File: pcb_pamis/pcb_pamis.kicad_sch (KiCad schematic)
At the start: 55 parts, among them J1 USB_C_Receptacle_USB2.0_16P, J10 Conn_01x03, J11 Conn_01x03, J12 Conn_02x06_Odd_Even, J13 1755736, J2 1755736, J6 Conn_01x05, J7 Conn_01x05, J8 Conn_01x05, J9 Conn_01x03, Q1 Q_NPN_BEC, Q2 Q_NPN_BEC, Q3 NMOS, Q4 NMOS, Q5 NMOS, SW1 SW_Push, U1 ESP32-WROOM-32UE, U2 CP2102N-Axx-xQFN28

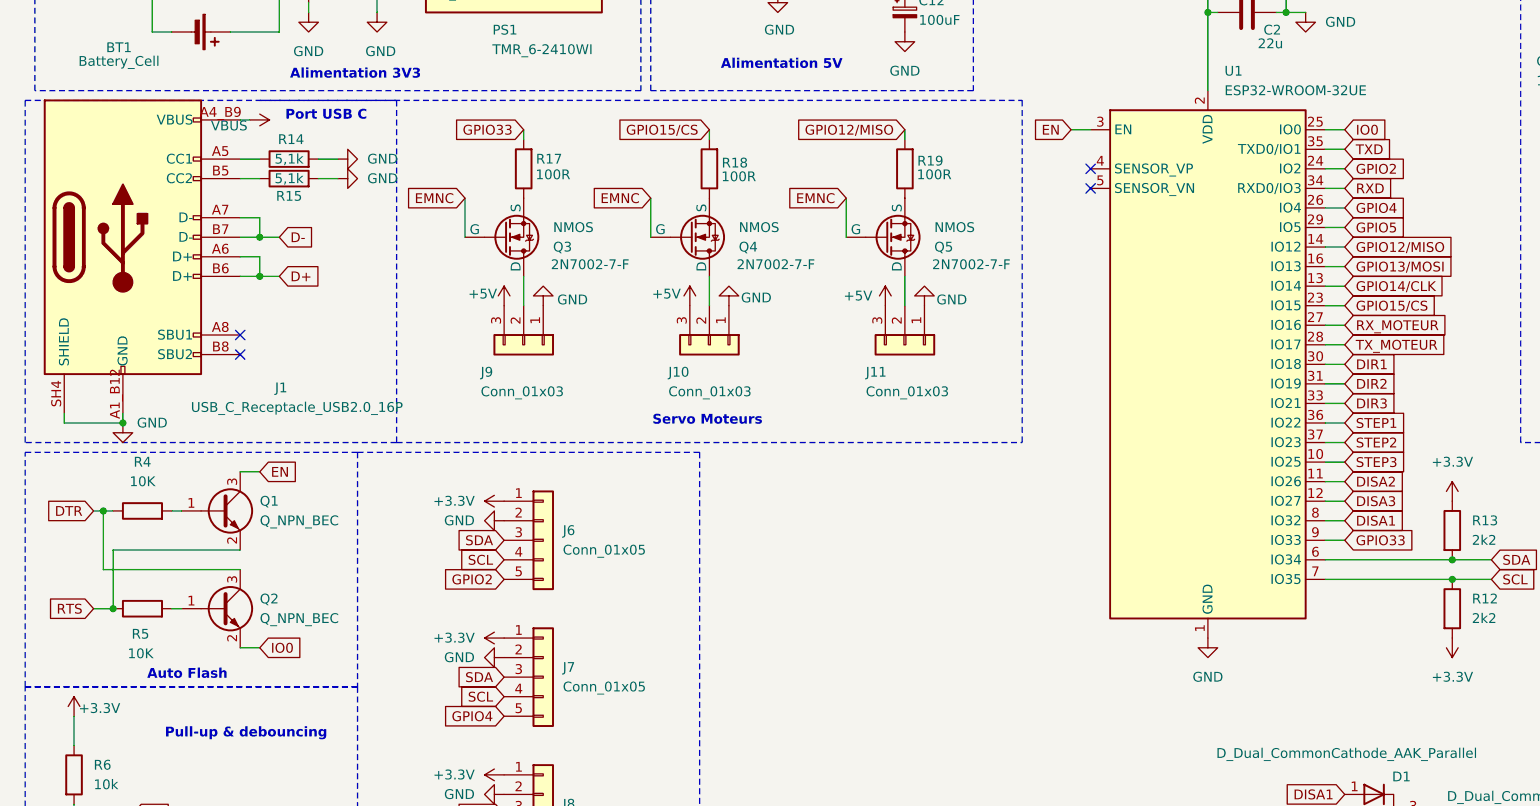
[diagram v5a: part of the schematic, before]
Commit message: correctif auto flash pcb pami
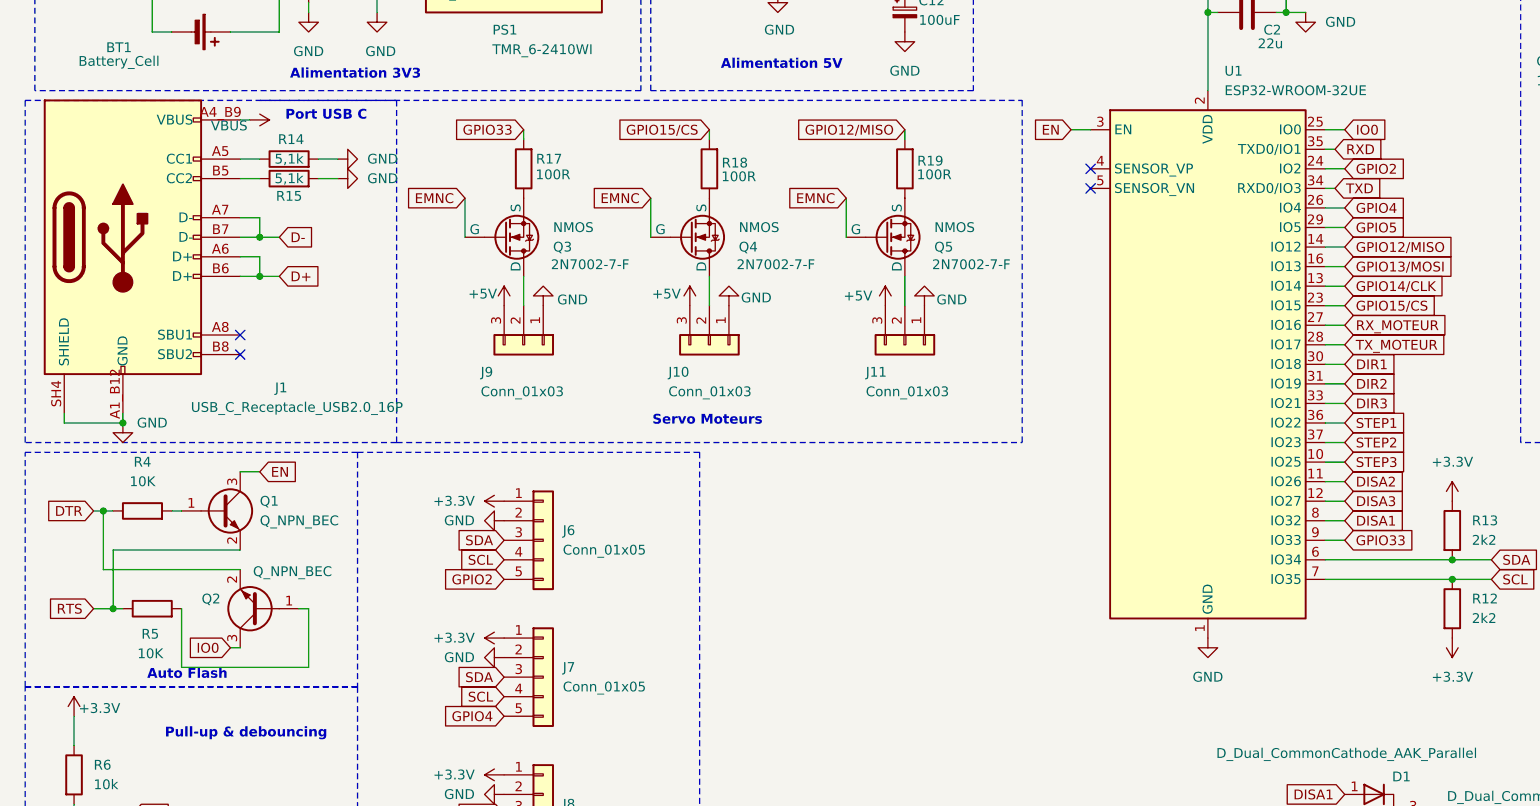
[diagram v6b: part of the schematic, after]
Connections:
- net DTR: now also Q2.2 (E); no longer Q2.3 (C)
- net IO0: now also Q2.3 (C); no longer Q2.2 (E)
- net RXD: now also U1.35 (TXD0/IO1); no longer U1.34 (RXD0/IO3)
- net TXD: now also U1.34 (RXD0/IO3); no longer U1.35 (TXD0/IO1)
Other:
- moved on the sheet: Q2, R5
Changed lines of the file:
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@@
 	(wire
 		(pts
-			(xy 182.88 60.96) (xy 185.42 60.96)
-		)
-		(stroke
-			(width 0)
-			(type default)
-		)
-	)
-	(wire
-		(pts
 			(xy 257.81 22.86) (xy 257.81 19.05)
 		)
@@
 	(wire
 		(pts
+			(xy 182.88 66.04) (xy 184.15 66.04)
+		)
+		(stroke
+			(width 0)
+			(type default)
+		)
+	)
+	(wire
+		(pts
 			(xy 22.86 191.77) (xy 22.86 193.04)
 		)
@@
 	(wire
 		(pts
-			(xy 41.91 125.73) (xy 44.45 125.73)
+			(xy 182.88 83.82) (xy 185.42 83.82)
 		)
 		(stroke
@@
 	(wire
 		(pts
-			(xy 182.88 83.82) (xy 185.42 83.82)
+			(xy 40.64 125.73) (xy 41.91 125.73)
 		)
 		(stroke
@@
 	(wire
 		(pts
+			(xy 50.8 120.65) (xy 50.8 128.27)
+		)
+		(stroke
+			(width 0)
+			(type default)
+		)
+	)
+	(wire
+		(pts
 			(xy 200.66 160.02) (xy 200.66 154.94)
 		)
@@
 	(wire
 		(pts
-			(xy 41.91 115.57) (xy 24.13 115.57)
-		)
-		(stroke
-			(width 0)
-			(type default)
-		)
-	)
-	(wire
-		(pts
 			(xy 128.27 40.64) (xy 128.27 36.83)
 		)
@@
 	(wire
 		(pts
+			(xy 50.8 128.27) (xy 34.29 128.27)
+		)
+		(stroke
+			(width 0)
+			(type default)
+		)
+	)
+	(wire
+		(pts
 			(xy 182.88 149.86) (xy 158.75 149.86)
 		)
@@
 	(wire
 		(pts
-			(xy 182.88 66.04) (xy 185.42 66.04)
+			(xy 182.88 60.96) (xy 184.15 60.96)
 		)
 		(stroke
@@
 	(wire
 		(pts
+			(xy 24.13 115.57) (xy 41.91 115.57)
+		)
+		(stroke
+			(width 0)
+			(type default)
+		)
+	)
+	(wire
+		(pts
 			(xy 185.42 68.58) (xy 182.88 68.58)
 		)
@@
 	(wire
 		(pts
+			(xy 34.29 128.27) (xy 34.29 120.65)
+		)
+		(stroke
+			(width 0)
+			(type default)
+		)
+	)
+	(wire
+		(pts
+			(xy 26.67 120.65) (xy 25.4 120.65)
+		)
+		(stroke
+			(width 0)
+			(type default)
+		)
+	)
+	(wire
+		(pts
 			(xy 78.74 58.42) (xy 78.74 59.69)
 		)
@@
 	(wire
 		(pts
-			(xy 33.02 120.65) (xy 34.29 120.65)
-		)
-		(stroke
-			(width 0)
-			(type default)
-		)
-	)
-	(wire
-		(pts
 			(xy 265.43 22.86) (xy 265.43 26.67)
 		)
@@
 	(wire
 		(pts
+			(xy 49.53 120.65) (xy 50.8 120.65)
+		)
+		(stroke
+			(width 0)
+			(type default)
+		)
+	)
+	(wire
+		(pts
 			(xy 232.41 157.48) (xy 231.14 157.48)
 		)
@@
 	(global_label "IO0"
 		(shape input)
-		(at 44.45 125.73 0)
+		(at 40.64 125.73 180)
 		(fields_autoplaced yes)
 		(effects
@@
 				(size 1.27 1.27)
 			)
-			(justify left)
+			(justify right)
 		)
 		(property "Intersheetrefs" "${INTERSHEET_REFS}"
-			(at 50.58 125.73 0)
+			(at 34.51 125.73 0)
 			(effects
 				(font
 					(size 1.27 1.27)
 				)
-				(justify left)
+				(justify right)
 				(hide yes)
 			)
@@
 	(global_label "TXD"
 		(shape input)
-		(at 185.42 60.96 0)
+		(at 184.15 66.04 0)
 		(fields_autoplaced yes)
 		(effects
@@
 		)
 		(property "Intersheetrefs" "${INTERSHEET_REFS}"
-			(at 191.8523 60.96 0)
+			(at 190.5823 66.04 0)
 			(effects
 				(font
@@
 	(global_label "RXD"
 		(shape input)
-		(at 185.42 66.04 0)
+		(at 184.15 60.96 0)
 		(fields_autoplaced yes)
 		(effects
@@
 		)
 		(property "Intersheetrefs" "${INTERSHEET_REFS}"
-			(at 192.1547 66.04 0)
+			(at 190.8847 60.96 0)
 			(effects
 				(font
@@
 	(symbol
 		(lib_id "Device:R")
-		(at 29.21 120.65 90)
+		(at 30.48 120.65 90)
 		(unit 1)
 		(exclude_from_sim no)
@@
 		(dnp no)
 		(property "Reference" "R5"
-			(at 28.956 123.952 90)
+			(at 30.226 123.952 90)
 			(effects
 				(font
@@
 		)
 		(property "Value" "10K"
-			(at 28.956 126.492 90)
+			(at 30.226 126.492 90)
 			(effects
 				(font
@@
 		)
 		(property "Footprint" "Resistor_SMD:R_0805_2012Metric_Pad1.20x1.40mm_HandSolder"
-			(at 29.21 122.428 90)
+			(at 30.48 122.428 90)
 			(effects
 				(font
@@
 		)
 		(property "Datasheet" "~"
-			(at 29.21 120.65 0)
+			(at 30.48 120.65 0)
 			(effects
 				(font
@@
 		)
 		(property "Description" "Resistor"
-			(at 29.21 120.65 0)
+			(at 30.48 120.65 0)
 			(effects
 				(font
@@
 		)
 		(property "MAXIMUM_PACKAGE_HEIGHT" ""
-			(at 29.21 120.65 0)
+			(at 30.48 120.65 0)
 			(effects
 				(font
@@
 	(symbol
 		(lib_id "Transistor_BJT:Q_NPN_BEC")
-		(at 39.37 120.65 0)
+		(at 44.45 120.65 180)
 		(unit 1)
 		(exclude_from_sim no)
@@
 		(on_board yes)
 		(dnp no)
-		(fields_autoplaced yes)
 		(property "Reference" "Q2"
-			(at 44.45 119.3799 0)
+			(at 39.37 119.3799 0)
 			(effects
 				(font
@@
 		)
 		(property "Value" "Q_NPN_BEC"
-			(at 44.45 121.9199 0)
+			(at 53.848 115.824 0)
 			(effects
 				(font
@@
 		)
 		(property "Footprint" "Package_TO_SOT_SMD:SOT-23_Handsoldering"
-			(at 44.45 118.11 0)
+			(at 39.37 123.19 0)
 			(effects
 				(font
@@
 		)
 		(property "Datasheet" "~"
-			(at 39.37 120.65 0)
+			(at 44.45 120.65 0)
 			(effects
 				(font
@@
 		)
 		(property "Description" "NPN transistor, base/emitter/collector"
-			(at 39.37 120.65 0)
+			(at 44.45 120.65 0)
 			(effects
 				(font
@@
 		)
 		(property "MAXIMUM_PACKAGE_HEIGHT" ""
-			(at 39.37 120.65 0)
+			(at 44.45 120.65 0)
 			(effects
 				(font
